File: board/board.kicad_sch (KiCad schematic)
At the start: 3 parts, among them J1 010_UART, J2 008_USB

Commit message: finished layout
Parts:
- added R6: 0R, Resistor_SMD:R_0603_1608Metric, symbol Device:R_Small
- J1: footprint (none) -> on_edge:on_edge_2x05_host
- J2: footprint (none) -> on_edge:on_edge_2x05_device
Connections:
- net +5V: now also R6.1
- net GND: now also J1.1 (GND)
- net cp2102/USB_VBUS: now also R6.2
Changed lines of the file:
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@@
   (junction (at 134.62 120.65) (diameter 0) (color 0 0 0 0)
+  )
+  (junction (at 134.62 97.79) (diameter 0) (color 0 0 0 0)
+  )
+  (junction (at 142.875 102.87) (diameter 0) (color 0 0 0 0)
   )
   (no_connect (at 198.12 110.49))
@@
     (stroke (width 0) (type default))
   )
+  (wire (pts (xy 142.875 102.87) (xy 148.59 102.87))
+    (stroke (width 0) (type default))
+  )
   (wire (pts (xy 198.12 120.65) (xy 194.945 120.65))
     (stroke (width 0) (type default))
@@
     (stroke (width 0) (type default))
   )
-  (wire (pts (xy 134.62 89.535) (xy 134.62 120.65))
+  (wire (pts (xy 134.62 97.79) (xy 134.62 120.65))
+    (stroke (width 0) (type default))
+  )
+  (wire (pts (xy 134.62 89.535) (xy 134.62 97.79))
     (stroke (width 0) (type default))
   )
@@
     (stroke (width 0) (type default))
   )
+  (wire (pts (xy 141.605 97.79) (xy 142.875 97.79))
+    (stroke (width 0) (type default))
+  )
   (wire (pts (xy 194.945 118.11) (xy 198.12 118.11))
     (stroke (width 0) (type default))
@@
     (stroke (width 0) (type default))
   )
+  (wire (pts (xy 134.62 97.79) (xy 136.525 97.79))
+    (stroke (width 0) (type default))
+  )
   (wire (pts (xy 175.26 102.87) (xy 198.12 102.87))
     (stroke (width 0) (type default))
   )
+  (wire (pts (xy 142.875 97.79) (xy 142.875 102.87))
+    (stroke (width 0) (type default))
+  )
   (wire (pts (xy 175.26 98.425) (xy 194.945 98.425))
     (stroke (width 0) (type default))
@@
     (stroke (width 0) (type default))
   )
-  (wire (pts (xy 132.715 102.87) (xy 148.59 102.87))
+  (wire (pts (xy 132.715 102.87) (xy 142.875 102.87))
+    (stroke (width 0) (type default))
+  )
+  (wire (pts (xy 208.28 125.73) (xy 208.28 128.905))
     (stroke (width 0) (type default))
   )
@@
       (effects (font (size 1.27 1.27)) (justify left))
     )
-    (property "Footprint" "" (at 217.17 95.25 0)
+    (property "Footprint" "on_edge:on_edge_2x05_host" (at 217.17 95.25 0)
       (effects (font (size 1.27 1.27)) hide)
     )
@@
     )
   )
+  (symbol (lib_id "power:GND") (at 208.28 128.905 0) (unit 1)
+    (in_bom yes) (on_board yes) (dnp no) (fields_autoplaced)
+    (property "Reference" "#PWR04" (at 208.28 135.255 0)
+      (effects (font (size 1.27 1.27)) hide)
+    )
+    (property "Value" "GND" (at 208.28 133.985 0)
+      (effects (font (size 1.27 1.27)))
+    )
+    (property "Footprint" "" (at 208.28 128.905 0)
+      (effects (font (size 1.27 1.27)) hide)
+    )
+    (property "Datasheet" "" (at 208.28 128.905 0)
+      (effects (font (size 1.27 1.27)) hide)
+    )
+    (pin "1")
+    (instances
+      (project "board"
+        (path "/57732dd3-1162-4c3f-88bd-31bf473d124d"
+          (reference "#PWR04") (unit 1)
+        )
+      )
+    )
+  )
   (symbol (lib_id "power:+3.3V") (at 194.945 96.52 0) (unit 1)
     (in_bom yes) (on_board yes) (dnp no) (fields_autoplaced)
@@
   (symbol (lib_id "power:GND") (at 182.88 139.7 0) (unit 1)
     (in_bom yes) (on_board yes) (dnp no) (fields_autoplaced)
-    (property "Reference" "#PWR?" (at 182.88 146.05 0)
+    (property "Reference" "#PWR0101" (at 182.88 146.05 0)
       (effects (font (size 1.27 1.27)) hide)
     )
@@
       (project "board"
         (path "/57732dd3-1162-4c3f-88bd-31bf473d124d"
-          (reference "#PWR?") (unit 1)
+          (reference "#PWR0101") (unit 1)
         )
       )
@@
       (effects (font (size 1.27 1.27)))
     )
-    (property "Footprint" "" (at 113.665 93.98 0)
+    (property "Footprint" "on_edge:on_edge_2x05_device" (at 113.665 93.98 0)
       (effects (font (size 1.27 1.27)) hide)
     )
@@
         )
       )
+    )
+  )
+  (symbol (lib_id "Device:R_Small") (at 139.065 97.79 90) (unit 1)
+    (in_bom yes) (on_board yes) (dnp yes) (fields_autoplaced)
+    (property "Reference" "R6" (at 139.065 92.075 90)
+      (effects (font (size 1.27 1.27)))
+    )
+    (property "Value" "0R" (at 139.065 94.615 90)
+      (effects (font (size 1.27 1.27)))
+    )
+    (property "Footprint" "Resistor_SMD:R_0603_1608Metric" (at 139.065 97.79 0)
+      (effects (font (size 1.27 1.27)) hide)
+    )
+    (property "Datasheet" "~" (at 139.065 97.79 0)
+      (effects (font (size 1.27 1.27)) hide)
+    )
+    (pin "1")
+    (pin "2")
+    (instances
+      (project "board"
+        (path "/57732dd3-1162-4c3f-88bd-31bf473d124d/767ce4c6-0e55-4543-92f0-34cb8237a544"
+          (reference "R6") (unit 1)
+        )
+        (path "/57732dd3-1162-4c3f-88bd-31bf473d124d"
+          (reference "R4") (unit 1)
+        )
+      )

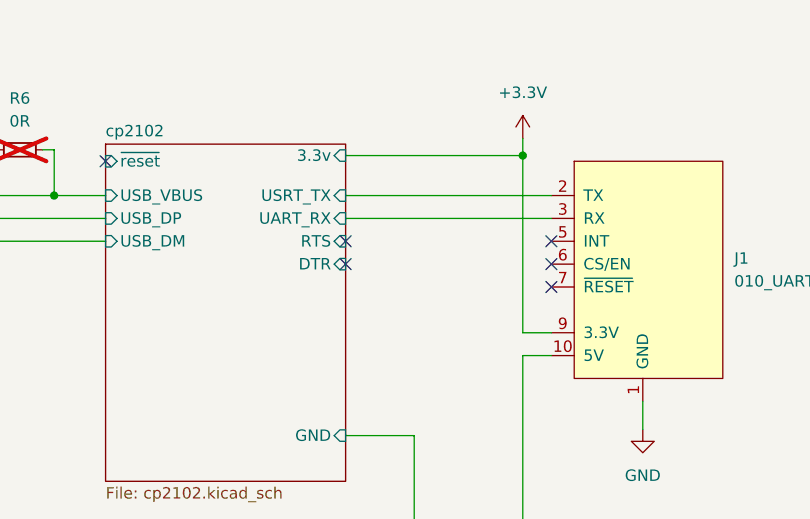
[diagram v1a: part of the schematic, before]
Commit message: added lcsc numbers
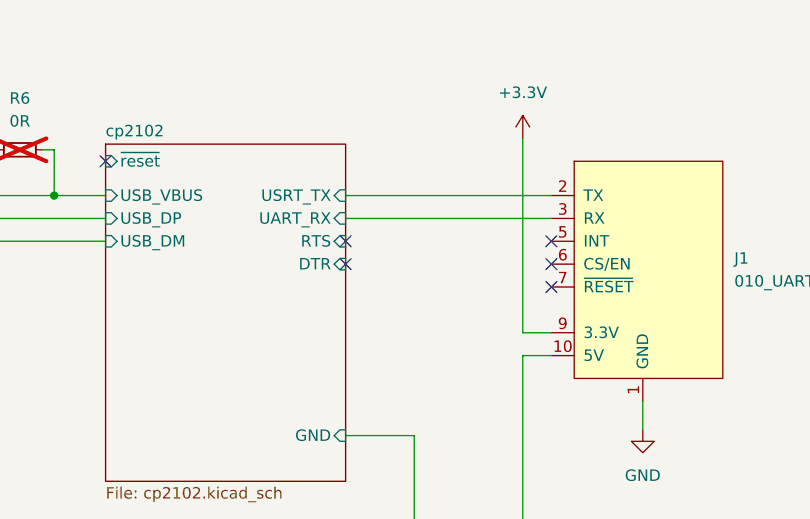
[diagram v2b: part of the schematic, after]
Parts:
- R6: footprint Resistor_SMD:R_0603_1608Metric -> Resistor_SMD:R_0402_1005Metric; lcsc (none) -> C17168
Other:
- sheet cp2102 ports: added none; removed 3.3v
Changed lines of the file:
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@@
 (kicad_sch (version 20230121) (generator eeschema)
   (paper "A4")
-  (junction (at 194.945 98.425) (diameter 0) (color 0 0 0 0)
-  )
   (junction (at 134.62 120.65) (diameter 0) (color 0 0 0 0)
   )
@@
   (no_connect (at 132.715 115.57))
   (no_connect (at 132.715 110.49))
-  (wire (pts (xy 194.945 98.425) (xy 194.945 118.11))
-    (stroke (width 0) (type default))
-  )
   (wire (pts (xy 132.715 105.41) (xy 148.59 105.41))
     (stroke (width 0) (type default))
@@
     (stroke (width 0) (type default))
   )
-  (wire (pts (xy 175.26 98.425) (xy 194.945 98.425))
-    (stroke (width 0) (type default))
-  )
   (wire (pts (xy 175.26 129.54) (xy 182.88 129.54))
     (stroke (width 0) (type default))
@@
     (stroke (width 0) (type default))
   )
-  (wire (pts (xy 194.945 96.52) (xy 194.945 98.425))
+  (wire (pts (xy 194.945 96.52) (xy 194.945 118.11))
     (stroke (width 0) (type default))
   )
@@
       (effects (font (size 1.27 1.27)))
     )
-    (property "Footprint" "Resistor_SMD:R_0603_1608Metric" (at 139.065 97.79 0)
+    (property "Footprint" "Resistor_SMD:R_0402_1005Metric" (at 139.065 97.79 0)
       (effects (font (size 1.27 1.27)) hide)
     )
     (property "Datasheet" "~" (at 139.065 97.79 0)
+      (effects (font (size 1.27 1.27)) hide)
+    )
+    (property "lcsc" "C17168" (at 139.065 97.79 0)
       (effects (font (size 1.27 1.27)) hide)
     )
@@
       (effects (font (size 1.27 1.27)) (justify right))
     )
-    (pin "3.3v" input (at 175.26 98.425 0)
-      (effects (font (size 1.27 1.27)) (justify right))
-    )
